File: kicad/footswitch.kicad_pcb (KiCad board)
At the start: 2 copper layers, 93 x 35.7 mm, 70 parts, among them IC1 ATMEGA328P-A, P1 Atmega right, P2 Atmega top, P3 Programming header, P4 Atmega bottom, P5 Atmega left, P6 Pot hdr, Q1 BSS214NWH6327XTSA1, Q2 BSS214NWH6327XTSA1, SW1 SW_RST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

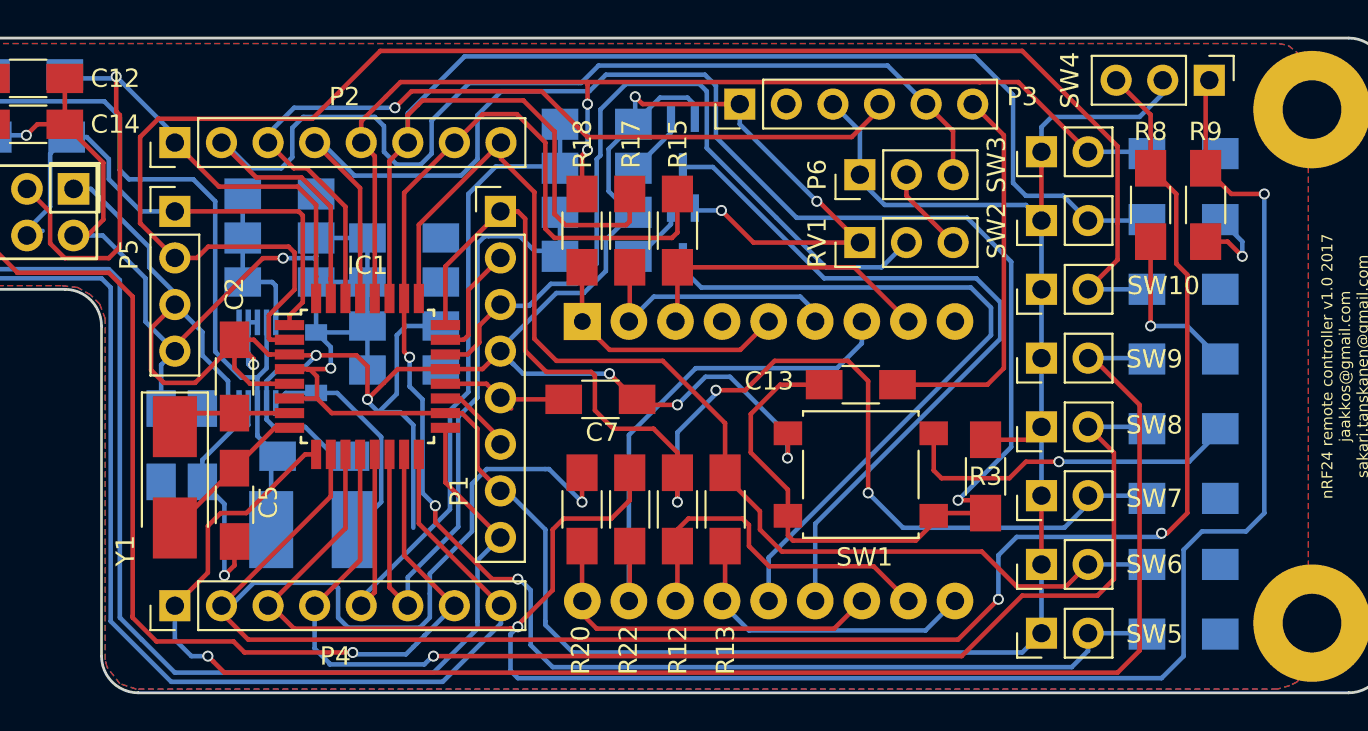
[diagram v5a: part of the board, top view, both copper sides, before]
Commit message: Add silk screen markings
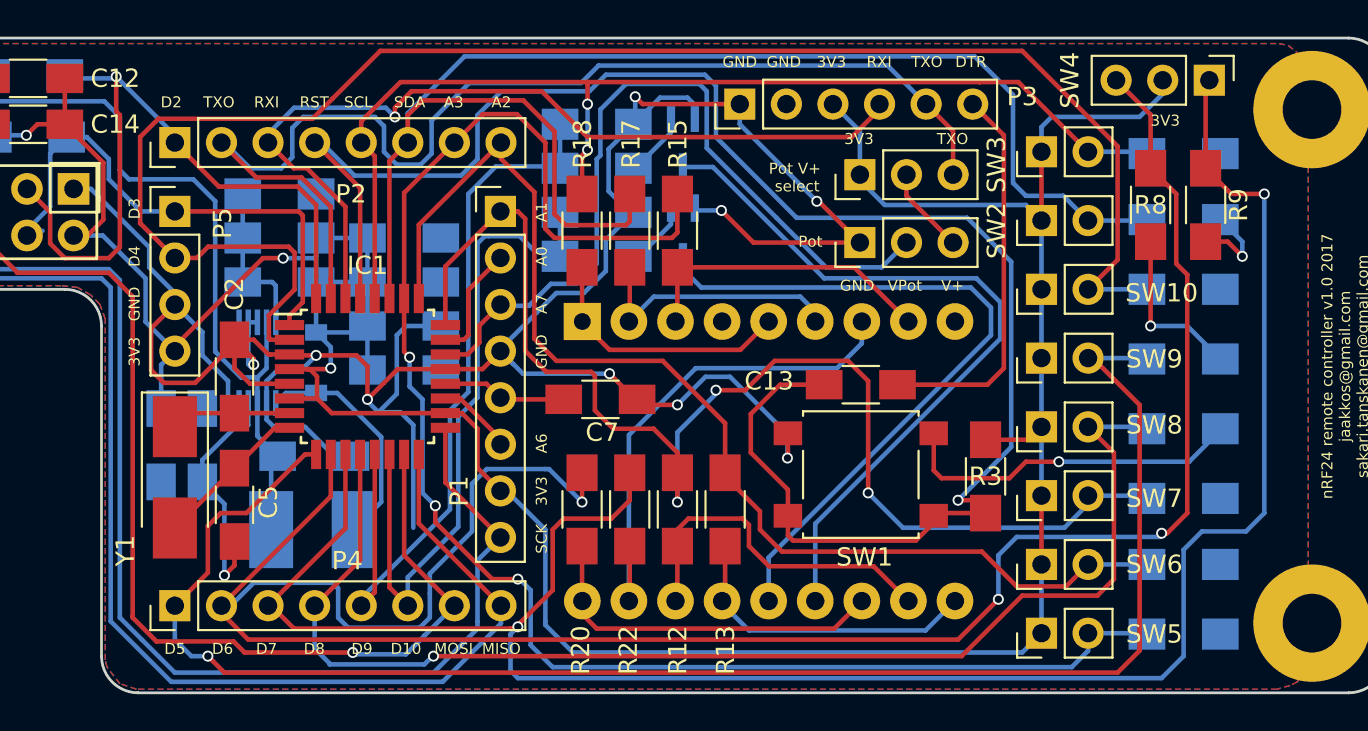
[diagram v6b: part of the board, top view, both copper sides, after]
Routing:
- net AREF: track 7.76 -> 6.93 mm
- net RXI: track 47.4 -> 48.1 mm
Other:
- board text added: "3V3"
- board text added: "A0"
- board text added: "A1"
- board text added: "A2"
- board text added: "A3"
- board text added: "A6"
- board text added: "A7"
- board text added: "D10"
- board text added: "D2"
- board text added: "D3"
- board text added: "D4"
- board text added: "D5"
- board text added: "D6"
- board text added: "D7"
- board text added: "D8"
- board text added: "D9"
- board text added: "DTR"
- board text added: "GND"
- board text added: "MISO"
- board text added: "MOSI"
- board text added: "Pot"
- board text added: "Pot V+ select"
- board text added: "RST"
- board text added: "RXI"
- board text added: "SCK"
- board text added: "SCL"
- board text added: "SDA"
- board text added: "TXO"
- board text added: "V+"
- board text added: "VPot"
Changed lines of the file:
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@@
     (area 16.924999 51.224999 110.075001 87.075001)
     (thickness 1.6)
-    (drawings 13)
-    (tracks 809)
+    (drawings 54)
+    (tracks 810)
     (zones 0)
     (modules 70)
@@
   (layers
     (0 F.Cu signal)
-    (31 B.Cu signal)
+    (31 B.Cu signal hide)
     (32 B.Adhes user)
     (33 F.Adhes user)
@@
     (pad_to_mask_clearance 0.2)
     (aux_axis_origin 0 0)
-    (visible_elements FFFEFF7F)
+    (visible_elements FFFE7F7F)
     (pcbplotparams
       (layerselection 0x00030_80000001)
@@
     (descr "Through hole straight pin header, 1x08, 2.54mm pitch, single row")
     (tags "Through hole pin header THT 1x08 2.54mm single row")
-    (fp_text reference P2 (at 2.5 9.25 180) (layer F.SilkS)
+    (fp_text reference P2 (at -2.8 9.6 180) (layer F.SilkS)
       (effects (font (size 1 1) (thickness 0.15)))
     )
@@
     (descr "Through hole straight pin header, 1x08, 2.54mm pitch, single row")
     (tags "Through hole pin header THT 1x08 2.54mm single row")
-    (fp_text reference P4 (at -2.75 8.75 180) (layer F.SilkS)
+    (fp_text reference P4 (at 2.45 9.4 180) (layer F.SilkS)
       (effects (font (size 1 1) (thickness 0.15)))
     )
@@
     (descr "Through hole straight pin header, 1x03, 2.54mm pitch, single row")
     (tags "Through hole pin header THT 1x03 2.54mm single row")
-    (fp_text reference P6 (at 0 -2.33 90) (layer F.SilkS)
+    (fp_text reference P6 (at 0 -2.33 90) (layer F.SilkS) hide
       (effects (font (size 1 1) (thickness 0.15)))
     )
@@
     (tags "resistor 1206")
     (attr smd)
-    (fp_text reference R8 (at 4 0 180) (layer F.SilkS)
+    (fp_text reference R8 (at 0 0 180) (layer F.SilkS)
       (effects (font (size 1 1) (thickness 0.15)))
     )
@@
     (tags "resistor 1206")
     (attr smd)
-    (fp_text reference R9 (at 4 0 360) (layer F.SilkS)
+    (fp_text reference R9 (at 0 1.8 90) (layer F.SilkS)
       (effects (font (size 1 1) (thickness 0.15)))
     )
@@
     (descr "Through hole straight pin header, 1x03, 2.54mm pitch, single row")
     (tags "Through hole pin header THT 1x03 2.54mm single row")
-    (fp_text reference RV1 (at 0 -2.33 90) (layer F.SilkS)
+    (fp_text reference RV1 (at 0 -2.33 90) (layer F.SilkS) hide
       (effects (font (size 1 1) (thickness 0.15)))
     )
@@
     (descr "Through hole straight pin header, 1x02, 2.54mm pitch, single row")
     (tags "Through hole pin header THT 1x02 2.54mm single row")
-    (fp_text reference SW10 (at 0.2 6.65 360) (layer F.SilkS)
+    (fp_text reference SW10 (at -0.2 6.55 360) (layer F.SilkS)
       (effects (font (size 1 1) (thickness 0.15)))
     )
@@
     (descr "Through hole straight pin header, 1x04, 2.54mm pitch, single row")
     (tags "Through hole pin header THT 1x04 2.54mm single row")
-    (fp_text reference P5 (at -2.5 2.35 90) (layer F.SilkS)
+    (fp_text reference P5 (at 2.6 0.65 90) (layer F.SilkS)
       (effects (font (size 1 1) (thickness 0.15)))
     )
@@
     (pad 1 thru_hole circle (at 0 0) (size 6.4 6.4) (drill 3.2) (layers *.Cu *.Mask))
   )
+  (gr_text TXO (at 86.4 56.8) (layer F.SilkS)
+    (effects (font (size 0.6 0.6) (thickness 0.1)))
+  )
+  (gr_text 3V3 (at 81.3 56.8) (layer F.SilkS)
+    (effects (font (size 0.6 0.6) (thickness 0.1)))
+  )
+  (gr_text 3V3 (at 98 55.8) (layer F.SilkS)
+    (effects (font (size 0.6 0.6) (thickness 0.1)))
+  )
+  (gr_text Pot (at 78.65 62.4) (layer F.SilkS)
+    (effects (font (size 0.6 0.6) (thickness 0.1)))
+  )
+  (gr_text "Pot V+\n select" (at 77.8 58.9) (layer F.SilkS)
+    (effects (font (size 0.6 0.6) (thickness 0.1)))
+  )
+  (gr_text V+ (at 86.4 64.8) (layer F.SilkS)
+    (effects (font (size 0.6 0.6) (thickness 0.1)))
+  )
+  (gr_text GND (at 81.2 64.8) (layer F.SilkS)
+    (effects (font (size 0.6 0.6) (thickness 0.1)))
+  )
+  (gr_text VPot (at 83.8 64.8) (layer F.SilkS)
+    (effects (font (size 0.6 0.6) (thickness 0.1)))
+  )
+  (gr_text DTR (at 87.4 52.6) (layer F.SilkS)
+    (effects (font (size 0.6 0.6) (thickness 0.1)))
+  )
+  (gr_text TXO (at 85 52.6) (layer F.SilkS)
+    (effects (font (size 0.6 0.6) (thickness 0.1)))
+  )
+  (gr_text RXI (at 82.4 52.6) (layer F.SilkS)
+    (effects (font (size 0.6 0.6) (thickness 0.1)))
+  )
+  (gr_text 3V3 (at 79.8 52.6) (layer F.SilkS)
+    (effects (font (size 0.6 0.6) (thickness 0.1)))
+  )
+  (gr_text GND (at 77.2 52.6) (layer F.SilkS)
+    (effects (font (size 0.6 0.6) (thickness 0.1)))
+  )
+  (gr_text GND (at 74.8 52.6) (layer F.SilkS)
+    (effects (font (size 0.6 0.6) (thickness 0.1)))
+  )
+  (gr_text A1 (at 64 60.8 90) (layer F.SilkS)
+    (effects (font (size 0.6 0.6) (thickness 0.1)))
+  )
+  (gr_text A0 (at 64 63.2 90) (layer F.SilkS)
+    (effects (font (size 0.6 0.6) (thickness 0.1)))
+  )
+  (gr_text A7 (at 64 65.8 90) (layer F.SilkS)
+    (effects (font (size 0.6 0.6) (thickness 0.1)))
+  )
+  (gr_text GND (at 64 68.4 90) (layer F.SilkS)
+    (effects (font (size 0.6 0.6) (thickness 0.1)))
+  )
+  (gr_text A6 (at 64 73.4 90) (layer F.SilkS)
+    (effects (font (size 0.6 0.6) (thickness 0.1)))
+  )
+  (gr_text 3V3 (at 64 76 90) (layer F.SilkS)
+    (effects (font (size 0.6 0.6) (thickness 0.1)))
+  )
+  (gr_text SCK (at 64 78.6 90) (layer F.SilkS)
+    (effects (font (size 0.6 0.6) (thickness 0.1)))
+  )
+  (gr_text MISO (at 61.8 84.6) (layer F.SilkS)
+    (effects (font (size 0.6 0.6) (thickness 0.1)))
+  )
+  (gr_text MOSI (at 59.2 84.6) (layer F.SilkS)
+    (effects (font (size 0.6 0.6) (thickness 0.1)))
+  )
+  (gr_text D10 (at 56.6 84.6) (layer F.SilkS)
+    (effects (font (size 0.6 0.6) (thickness 0.1)))
+  )
+  (gr_text D9 (at 54.2 84.6) (layer F.SilkS)
+    (effects (font (size 0.6 0.6) (thickness 0.1)))
+  )
+  (gr_text D8 (at 51.6 84.6) (layer F.SilkS)
+    (effects (font (size 0.6 0.6) (thickness 0.1)))
+  )
+  (gr_text D7 (at 49 84.6) (layer F.SilkS)
+    (effects (font (size 0.6 0.6) (thickness 0.1)))
+  )
+  (gr_text D6 (at 46.6 84.6) (layer F.SilkS)
+    (effects (font (size 0.6 0.6) (thickness 0.1)))
+  )
+  (gr_text D5 (at 44 84.6) (layer F.SilkS)
+    (effects (font (size 0.6 0.6) (thickness 0.1)))
+  )
+  (gr_text 3V3 (at 41.8 68.4 90) (layer F.SilkS)
+    (effects (font (size 0.6 0.6) (thickness 0.1)))
+  )
+  (gr_text GND (at 41.8 65.8 90) (layer F.SilkS)
+    (effects (font (size 0.6 0.6) (thickness 0.1)))
+  )
+  (gr_text D4 (at 41.8 63.2 90) (layer F.SilkS)
+    (effects (font (size 0.6 0.6) (thickness 0.1)))
+  )
+  (gr_text D3 (at 41.8 60.6 90) (layer F.SilkS)
+    (effects (font (size 0.6 0.6) (thickness 0.1)))
+  )
+  (gr_text A2 (at 61.8 54.8) (layer F.SilkS)
+    (effects (font (size 0.6 0.6) (thickness 0.1)))
+  )
+  (gr_text A3 (at 59.2 54.8) (layer F.SilkS)
+    (effects (font (size 0.6 0.6) (thickness 0.1)))
+  )
+  (gr_text SDA (at 56.8 54.8) (layer F.SilkS)
+    (effects (font (size 0.6 0.6) (thickness 0.1)))
+  )
+  (gr_text SCL (at 54 54.8) (layer F.SilkS)
+    (effects (font (size 0.6 0.6) (thickness 0.1)))
+  )
+  (gr_text RST (at 51.6 54.8) (layer F.SilkS)
+    (effects (font (size 0.6 0.6) (thickness 0.1)))
+  )
+  (gr_text RXI (at 49 54.8) (layer F.SilkS)
+    (effects (font (size 0.6 0.6) (thickness 0.1)))
+  )
+  (gr_text TXO (at 46.4 54.8) (layer F.SilkS)
+    (effects (font (size 0.6 0.6) (thickness 0.1)))
+  )
+  (gr_text D2 (at 43.8 54.8) (layer F.SilkS)
+    (effects (font (size 0.6 0.6) (thickness 0.1)))
+  )
   (gr_text "nRF24 remote controller v1.0 2017\njaakkos@gmail.com\nsakari.tanskanen@gmail.com" (at 107.8 69.2 90) (layer F.SilkS)
     (effects (font (size 0.6 0.6) (thickness 0.1)))
@@
   (segment (start 58.75 70.15) (end 60.99 70.15) (width 0.25) (layer F.Cu) (net 16))
   (segment (start 60.99 70.15) (end 61.75 70.91) (width 0.25) (layer F.Cu) (net 16))
-  (segment (start 62.34 71.5) (end 61.75 70.91) (width 0.25) (layer F.Cu) (net 16))
   (segment (start 61.84 71) (end 61.75 70.91) (width 0.25) (layer F.Cu) (net 16))
   (segment (start 79.9 61.1) (end 77.9 61.1) (width 0.25) (layer B.Cu) (net 17))
@@
   (segment (start 54.9 65.5) (end 54.9 57.74) (width 0.25) (layer F.Cu) (net 38))
   (segment (start 54.9 57.74) (end 54.16 57) (width 0.25) (layer F.Cu) (net 38))
-  (segment (start 49.08 57) (end 49.08 56.52) (width 0.25) (layer B.Cu) (net 39))
-  (segment (start 49.08 56.52) (end 50.5 55.1) (width 0.25) (layer B.Cu) (net 39))
-  (via (at 56 55.1) (size 0.6) (drill 0.4) (layers F.Cu B.Cu) (net 39))
-  (segment (start 56.9 54.2) (end 56 55.1) (width 0.25) (layer F.Cu) (net 39))
-  (segment (start 64 54.2) (end 56.9 54.2) (width 0.25) (layer F.Cu) (net 39))
-  (segment (start 66.5 56.7) (end 64 54.2) (width 0.25) (layer F.Cu) (net 39))
-  (segment (start 80.9 56.7) (end 66.5 56.7) (width 0.25) (layer F.Cu) (net 39))
+  (segment (start 56 55.6) (end 56 55.1) (width 0.25) (layer F.Cu) (net 39))
   (segment (start 82.42 55.18) (end 80.9 56.7) (width 0.25) (layer F.Cu) (net 39))
-  (segment (start 50.5 55.1) (end 56 55.1) (width 0.25) (layer B.Cu) (net 39))
+  (segment (start 80.9 56.7) (end 66.5 56.7) (width 0.25) (layer F.Cu) (net 39))
+  (segment (start 66.5 56.7) (end 64 54.2) (width 0.25) (layer F.Cu) (net 39))
+  (segment (start 64 54.2) (end 56.9 54.2) (width 0.25) (layer F.Cu) (net 39))
+  (segment (start 55.5 55.1) (end 56 55.6) (width 0.25) (layer B.Cu) (net 39))
+  (via (at 56 55.6) (size 0.6) (drill 0.4) (layers F.Cu B.Cu) (net 39))
+  (segment (start 50.5 55.1) (end 49.08 56.52) (width 0.25) (layer B.Cu) (net 39))
+  (segment (start 50.5 55.1) (end 55.5 55.1) (width 0.25) (layer B.Cu) (net 39))
+  (segment (start 56 55.1) (end 56.9 54.2) (width 0.25) (layer F.Cu) (net 39))
+  (segment (start 49.08 57) (end 49.08 56.52) (width 0.25) (layer B.Cu) (net 39))
   (segment (start 82.42 54.9) (end 82.42 55.18) (width 0.25) (layer F.Cu) (net 39))
   (segment (start 53.3 65.5) (end 53.3 60.5) (width 0.25) (layer F.Cu) (net 39))
